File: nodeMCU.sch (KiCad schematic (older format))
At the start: 34 parts, among them J1 USB_B_Micro, J2 Conn_01x15, J3 Conn_01x15, Q1 S8050, Q2 S8050, SW1 RESET, SW2 FLASH, U1 AP1117-33, U2 CP2102N-A01-GQFN28, U3 ESP-12E

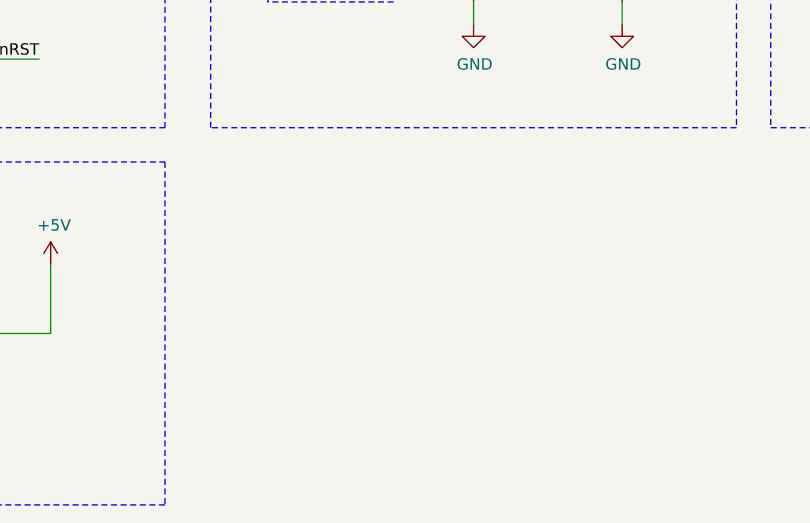
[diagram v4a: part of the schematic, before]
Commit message: Agrego agujeros de sujecion esquematico + pcb
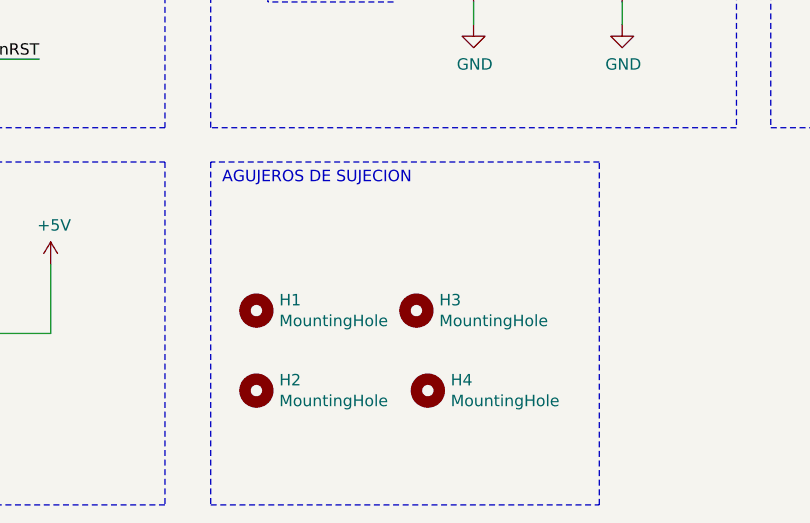
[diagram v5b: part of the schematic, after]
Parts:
- added H1, H2, H3, H4: MountingHole, MountingHole:MountingHole_2.2mm_M2, symbol Mechanical:MountingHole
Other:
- note added: "AGUJEROS DE SUJECION"
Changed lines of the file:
@@
 	-1   0    0    1
 $EndComp
+$Comp
+L Mechanical:MountingHole H1
+U 1 1 5D1E5AB6
+P 5350 6850
+F 0 "H1" H 5450 6896 50  0000 L CNN
+F 1 "MountingHole" H 5450 6805 50  0000 L CNN
+F 2 "MountingHole:MountingHole_2.2mm_M2" H 5350 6850 50  0001 C CNN
+F 3 "~" H 5350 6850 50  0001 C CNN
+	1    5350 6850
+	1    0    0    -1
+$EndComp
+$Comp
+L Mechanical:MountingHole H3
+U 1 1 5D1E5FD2
+P 6050 6850
+F 0 "H3" H 6150 6896 50  0000 L CNN
+F 1 "MountingHole" H 6150 6805 50  0000 L CNN
+F 2 "MountingHole:MountingHole_2.2mm_M2" H 6050 6850 50  0001 C CNN
+F 3 "~" H 6050 6850 50  0001 C CNN
+	1    6050 6850
+	1    0    0    -1
+$EndComp
+$Comp
+L Mechanical:MountingHole H2
+U 1 1 5D1E64ED
+P 5350 7200
+F 0 "H2" H 5450 7246 50  0000 L CNN
+F 1 "MountingHole" H 5450 7155 50  0000 L CNN
+F 2 "MountingHole:MountingHole_2.2mm_M2" H 5350 7200 50  0001 C CNN
+F 3 "~" H 5350 7200 50  0001 C CNN
+	1    5350 7200
+	1    0    0    -1
+$EndComp
+$Comp
+L Mechanical:MountingHole H4
+U 1 1 5D1E67FE
+P 6100 7200
+F 0 "H4" H 6200 7246 50  0000 L CNN
+F 1 "MountingHole" H 6200 7155 50  0000 L CNN
+F 2 "MountingHole:MountingHole_2.2mm_M2" H 6100 7200 50  0001 C CNN
+F 3 "~" H 6100 7200 50  0001 C CNN
+	1    6100 7200
+	1    0    0    -1
+$EndComp
+Wire Notes Line
+	5150 6200 5150 7700
+Wire Notes Line
+	5150 7700 6850 7700
+Wire Notes Line
+	6850 7700 6850 6200
+Wire Notes Line
+	6850 6200 5150 6200
+Text Notes 5200 6300 0    50   ~ 0
+AGUJEROS DE SUJECION
 $EndSCHEMATC

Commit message: Corrijo footprint de diodo D1
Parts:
- D1: footprint Diode_THT:D_DO-41_SOD81_P10.16mm_Horizontal -> Diode_SMD:D_SOD-323_HandSoldering
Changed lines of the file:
@@
 F 0 "D1" H 4050 6734 50  0000 C CNN
 F 1 "1N5819" H 4050 6825 50  0000 C CNN
-F 2 "Diode_THT:D_DO-41_SOD81_P10.16mm_Horizontal" H 4050 6775 50  0001 C CNN
+F 2 "Diode_SMD:D_SOD-323_HandSoldering" H 4050 6775 50  0001 C CNN
 F 3 "http://www.vishay.com/docs/88525/1n5817.pdf" H 4050 6950 50  0001 C CNN
 	1    4050 6950

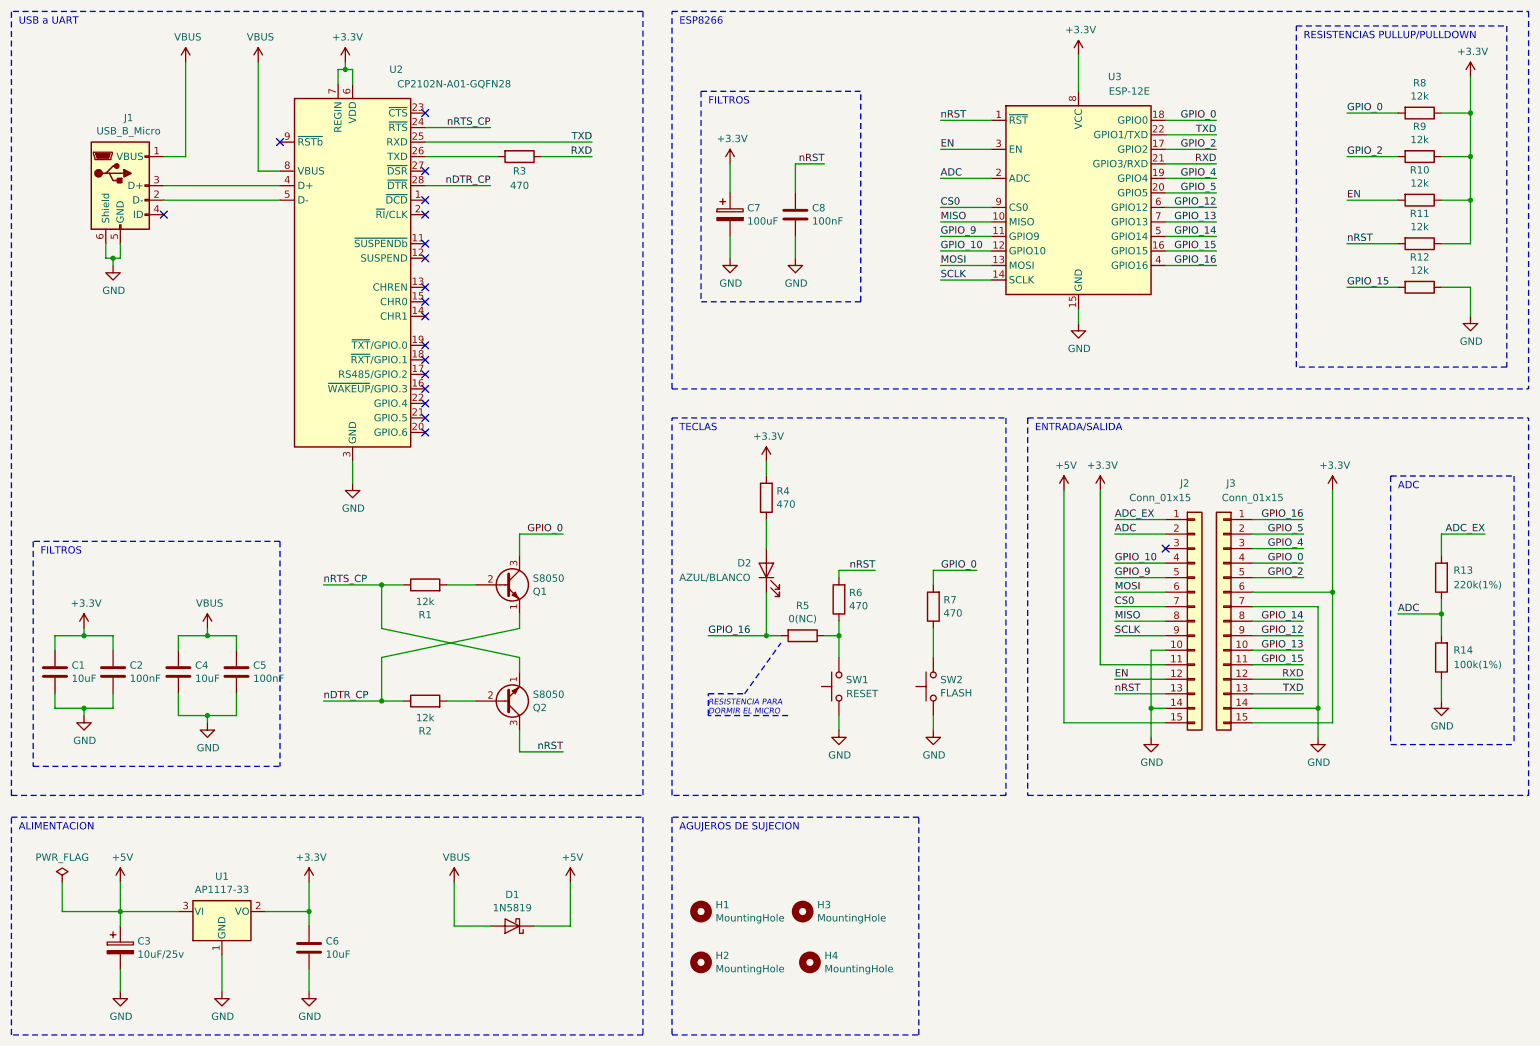
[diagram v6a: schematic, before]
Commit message: Cambios propuesto por el docente en el esquematico
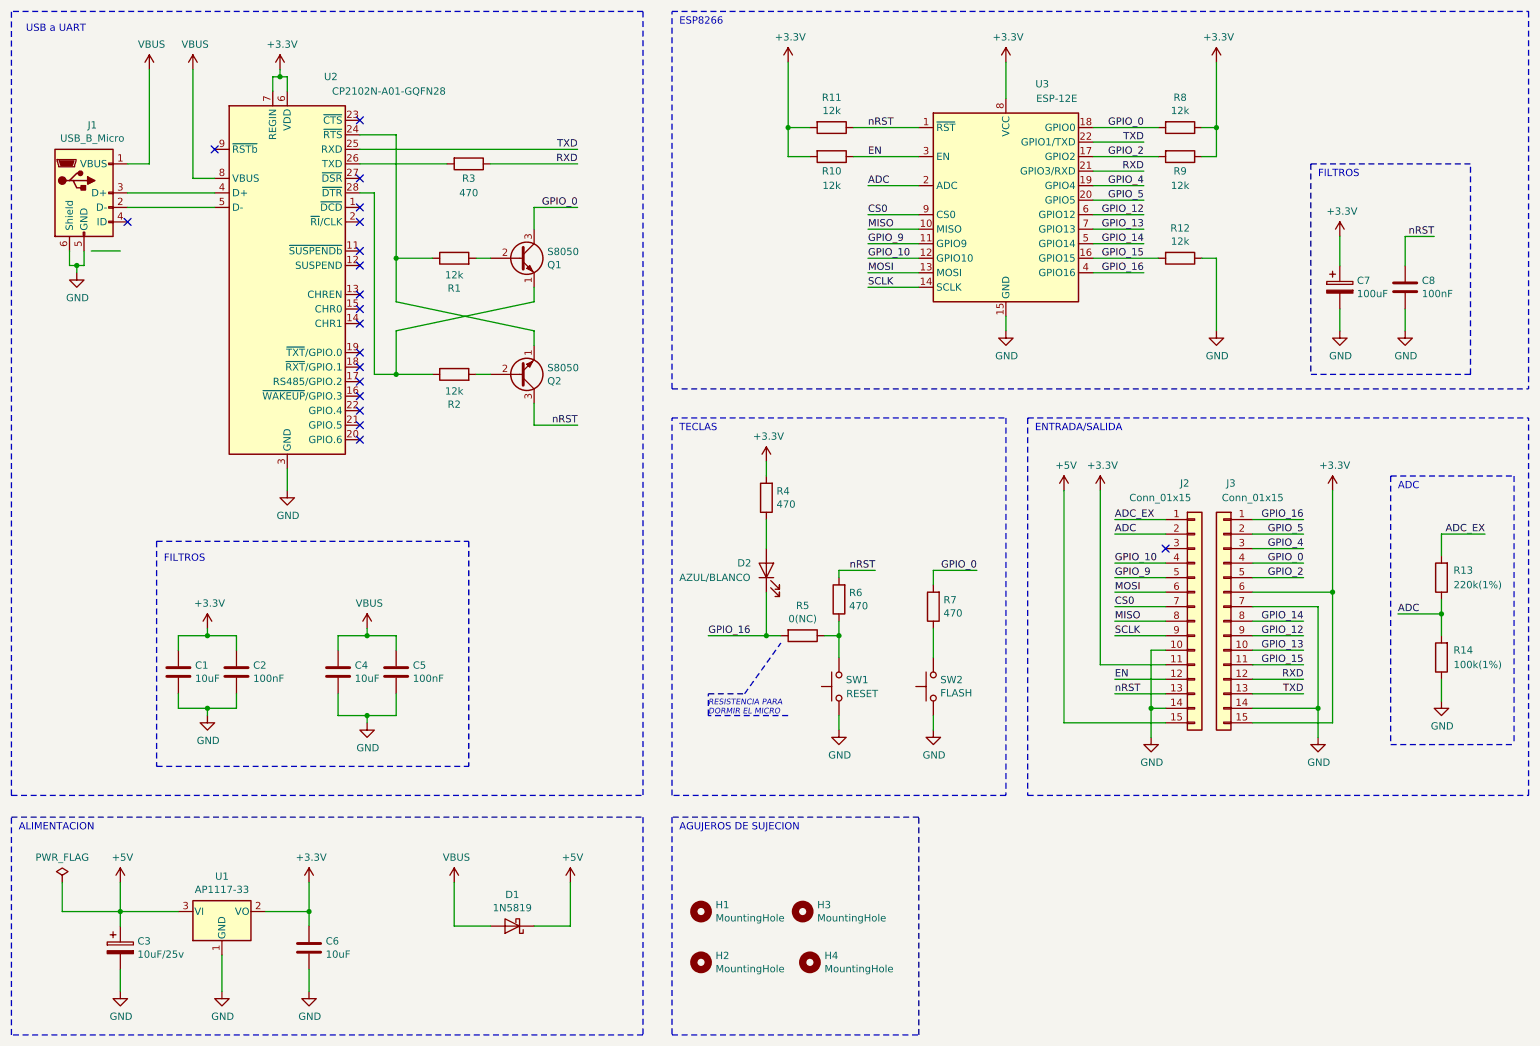
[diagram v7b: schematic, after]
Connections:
- net +3V3: now also R10.2, R11.2; no longer R10.1, R11.1
- net EN: now also R10.1; no longer R10.2
- net nRST: now also R11.1; no longer R11.2
- net nDTR_CP: no longer names the net of Q1.1 (E), R2.1, U2.28 (~DTR)
- net nRTS_CP: no longer names the net of Q2.1 (E), R1.1, U2.24 (~RTS)
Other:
- note removed: "RESISTENCIAS PULLUP/PULLDOWN"
- moved on the sheet: C1, C2, C4, C5, C7, C8, J1, Q1, Q2, R1, R10, R11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

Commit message: Borro ruteo
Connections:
- net +3V3: now also C1.2, C2.2; no longer C1.1, C2.1
- net GND: now also C1.1, C2.1, C8.1; no longer C1.2, C2.2, C8.2, J1.6 (Shield)
- net nRST: now also C8.2; no longer C8.1
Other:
- note added: "SALIDAS"
- note removed: "ADC"
- note removed: "ENTRADA/SALIDA"
- note removed: "FILTROS"
- moved on the sheet: C1, C2, C3, C4, C5, C6, C7, C8, D1, D2, H1, H2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
